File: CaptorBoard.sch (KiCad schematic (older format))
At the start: 55 parts, among them CON1 MINI-USB-SHELD-MC32598, P1 Prog, P2 POWER, Q1 IRLM6402TRPBF, SW1 CST06S08H, U1 PIC32MX795F512H-80I-PT, U2 MRF24J40MA-I-RM, U3 HTU21, U4 MPL115A2, U5 VTX-214-003-105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

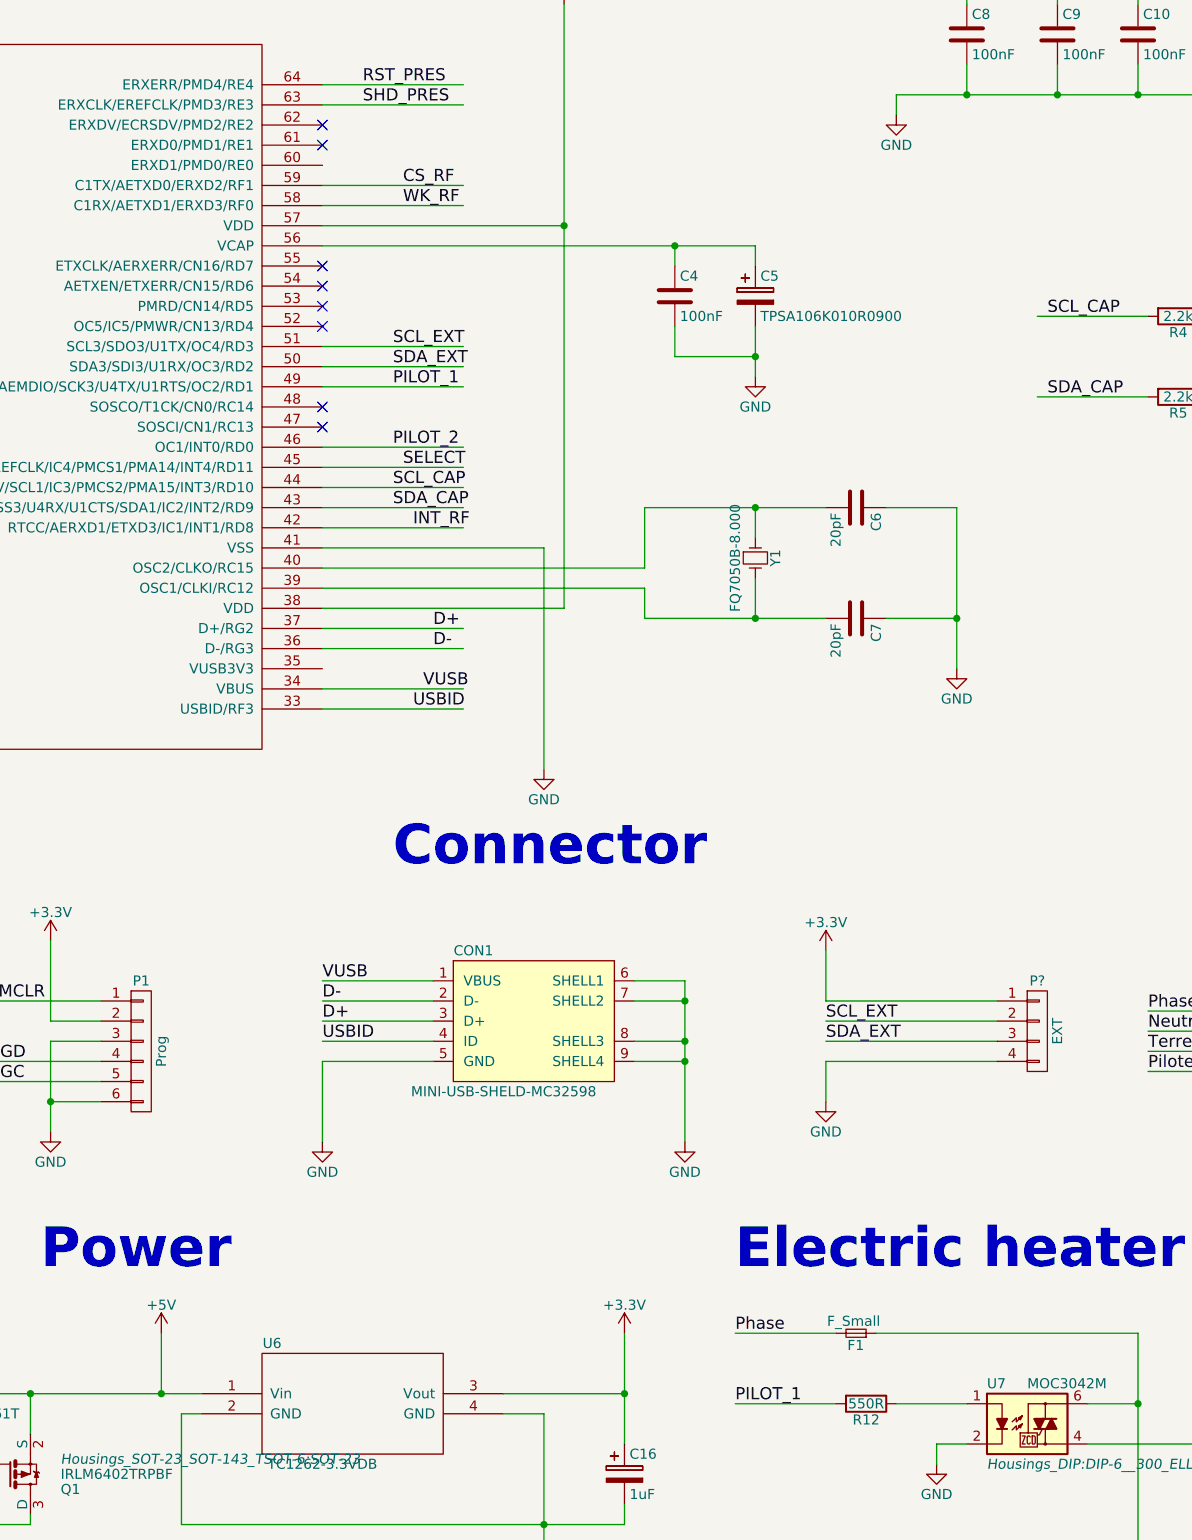
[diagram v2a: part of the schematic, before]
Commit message: Some ERC correction
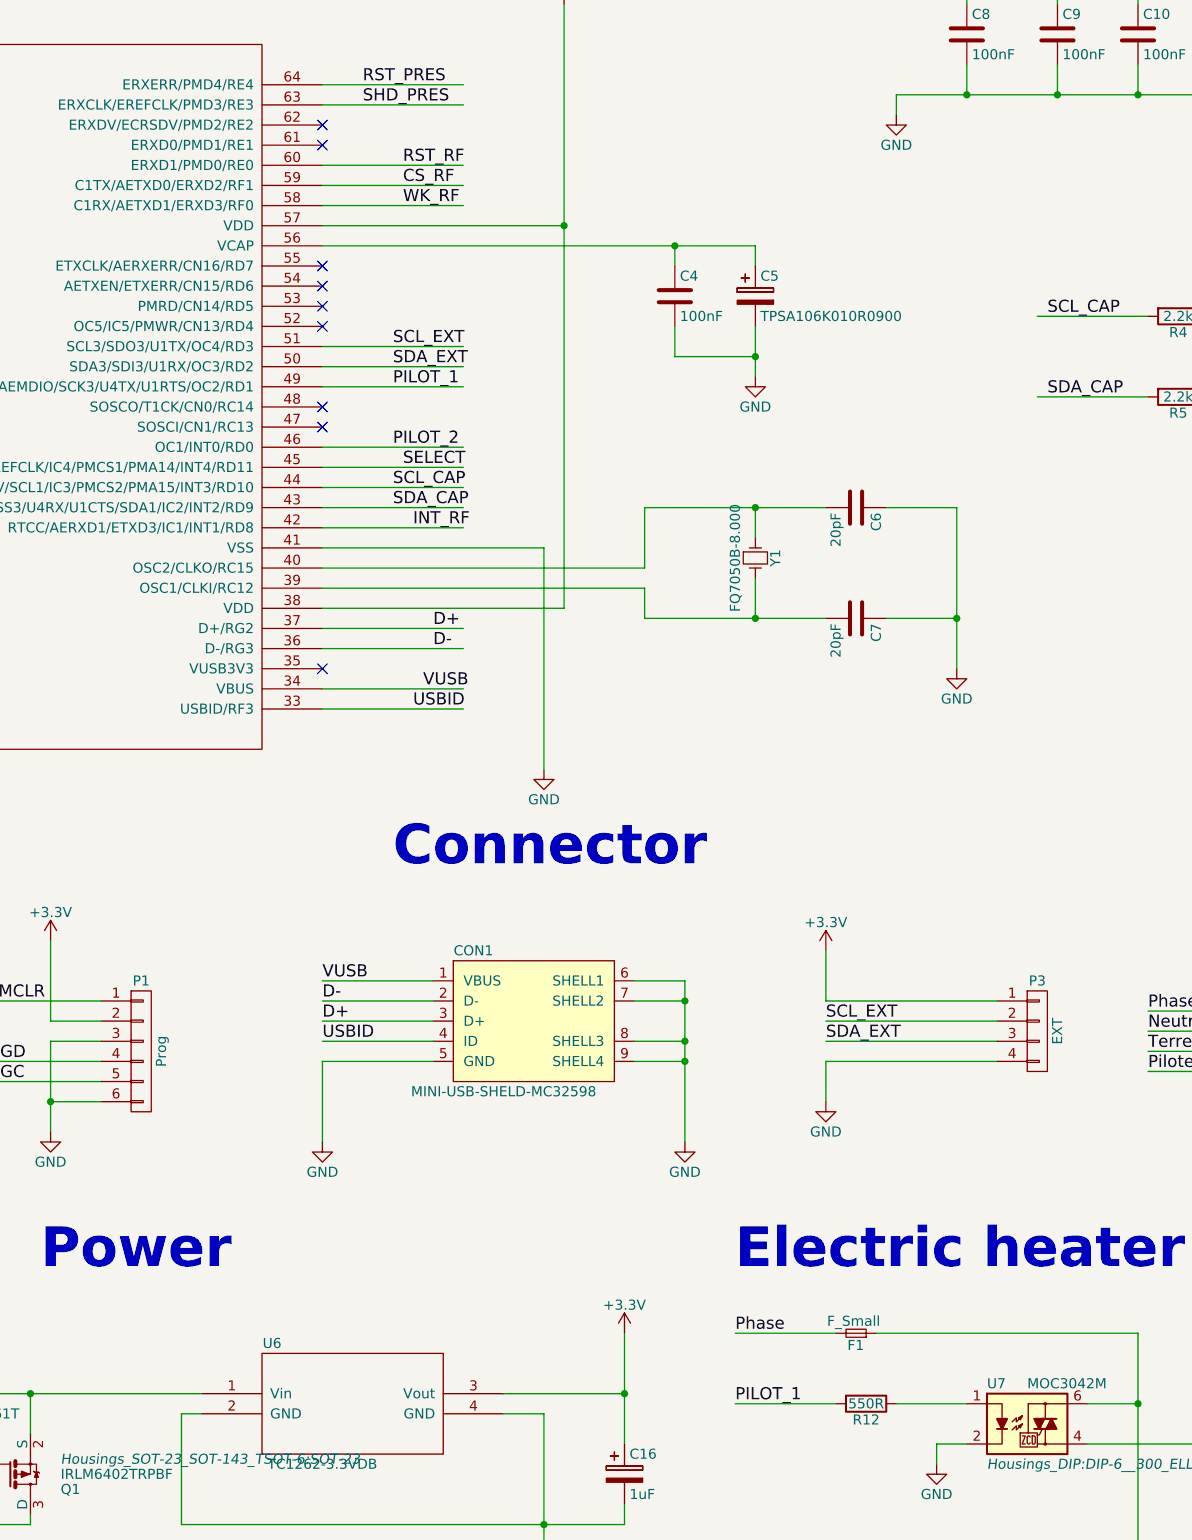
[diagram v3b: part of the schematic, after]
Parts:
- gave numbers to parts that had none: 1
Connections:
- net labels removed: +5V
- no-connect marks 23 -> 24
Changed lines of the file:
@@
-	1    0    0    -1
-$EndComp
-$Comp
-L +5V #PWR028
-U 1 1 5525FA48
-P 9800 7650
-F 0 "#PWR028" H 9800 7500 50  0001 C CNN
-F 1 "+5V" H 9800 7790 50  0000 C CNN
-F 2 "" H 9800 7650 60  0000 C CNN
-F 3 "" H 9800 7650 60  0000 C CNN
-	1    9800 7650
 	1    0    0    -1
 $EndComp
@@
 Power
 $Comp
-L GND #PWR029
+L GND #PWR028
 U 1 1 552620E9
 P 10900 10050
-F 0 "#PWR029" H 10900 9800 50  0001 C CNN
+F 0 "#PWR028" H 10900 9800 50  0001 C CNN
 F 1 "GND" H 10900 9900 50  0000 C CNN
 F 2 "" H 10900 10050 60  0000 C CNN
@@
 $EndComp
 $Comp
-L GND #PWR030
+L GND #PWR029
 U 1 1 55264B50
 P 13650 8300
-F 0 "#PWR030" H 13650 8050 50  0001 C CNN
+F 0 "#PWR029" H 13650 8050 50  0001 C CNN
 F 1 "GND" H 13650 8150 50  0000 C CNN
 F 2 "" H 13650 8300 60  0000 C CNN
@@
 $EndComp
 $Comp
-L GND #PWR031
+L GND #PWR030
 U 1 1 55264C81
 P 13650 9450
-F 0 "#PWR031" H 13650 9200 50  0001 C CNN
+F 0 "#PWR030" H 13650 9200 50  0001 C CNN
 F 1 "GND" H 13650 9300 50  0000 C CNN
 F 2 "" H 13650 9450 60  0000 C CNN
@@
 Wire Wire Line
 	9000 7950 10000 7950
-Wire Wire Line
-	9800 7950 9800 7650
-Connection ~ 9800 7950
 Wire Wire Line
 	9150 8150 9150 7950
@@
 Pilote
 $Comp
-L CONN_01X04 P?
+L CONN_01X04 P3
 U 1 1 5533F0E1
 P 14150 6150
-F 0 "P?" H 14150 6400 50  0000 C CNN
+F 0 "P3" H 14150 6400 50  0000 C CNN
 F 1 "EXT" V 14250 6150 50  0000 C CNN
 F 2 "" H 14150 6150 60  0000 C CNN
@@
 	13950 6300 13100 6300
 $Comp
-L GND #PWR?
+L GND #PWR031
 U 1 1 5533FC25
 P 13100 6500
-F 0 "#PWR?" H 13100 6250 50  0001 C CNN
+F 0 "#PWR031" H 13100 6250 50  0001 C CNN
 F 1 "GND" H 13100 6350 50  0000 C CNN
 F 2 "" H 13100 6500 60  0000 C CNN
@@
 $EndComp
 $Comp
-L +3.3V #PWR?
+L +3.3V #PWR032
 U 1 1 5533FE1F
 P 13100 5750
-F 0 "#PWR?" H 13100 5600 50  0001 C CNN
+F 0 "#PWR032" H 13100 5600 50  0001 C CNN
 F 1 "+3.3V" H 13100 5890 50  0000 C CNN
 F 2 "" H 13100 5750 60  0000 C CNN
@@
 Text Label 13100 6200 0    60   ~ 0
 SDA_EXT
+NoConn ~ 10600 4350
+Wire Wire Line
+	10600 1850 11300 1850
+Text Label 11000 1850 0    60   ~ 0
+RST_RF
 $EndSCHEMATC

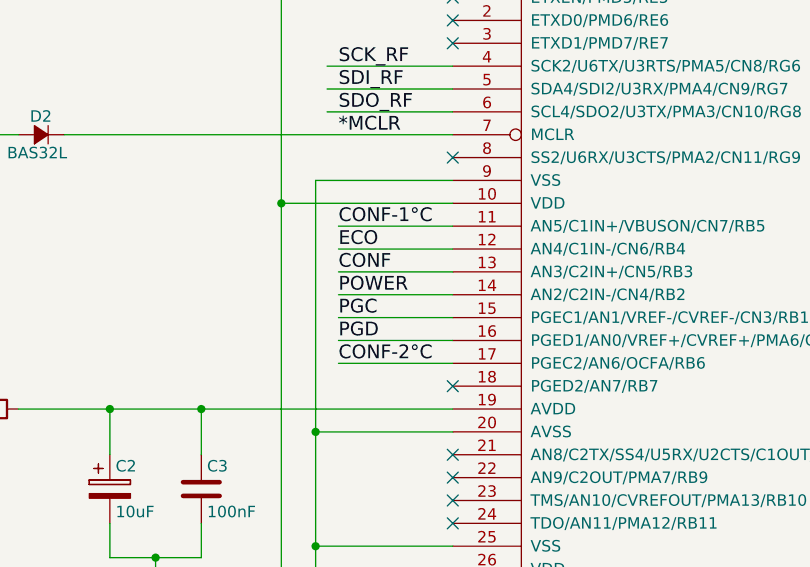
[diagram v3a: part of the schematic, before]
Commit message: Change led pin order for routing facility
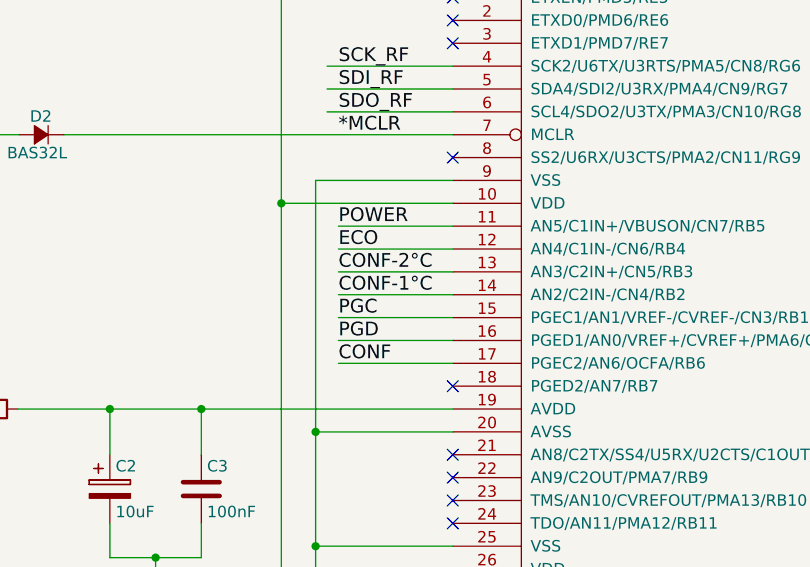
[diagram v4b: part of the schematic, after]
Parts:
- P3: footprint (none) -> Pin_Headers:Pin_Header_Straight_1x04
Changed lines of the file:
@@
 Text Label 3600 1950 0    60   ~ 0
 SDO_RF
-Text Label 3600 2450 0    60   ~ 0
+Text Label 3600 2750 0    60   ~ 0
 CONF-1°C
 Text Label 3600 2550 0    60   ~ 0
 ECO
-Text Label 3600 2650 0    60   ~ 0
+Text Label 3600 3050 0    60   ~ 0
 CONF
-Text Label 3600 2750 0    60   ~ 0
+Text Label 3600 2450 0    60   ~ 0
 POWER
 Text Label 3600 2850 0    60   ~ 0
@@
 Text Label 3600 2950 0    60   ~ 0
 PGD
-Text Label 3600 3050 0    60   ~ 0
+Text Label 3600 2650 0    60   ~ 0
 CONF-2°C
 NoConn ~ 4100 1450
@@
 	4100 1950 3550 1950
 Wire Wire Line
+	4100 2750 3600 2750
+Wire Wire Line
+	4100 2550 3600 2550
+Wire Wire Line
+	4100 3050 3600 3050
+Wire Wire Line
 	4100 2450 3600 2450
 Wire Wire Line
-	4100 2550 3600 2550
+	4100 2850 3600 2850
+Wire Wire Line
+	4100 2950 3600 2950
 Wire Wire Line
 	4100 2650 3600 2650
-Wire Wire Line
-	4100 2750 3600 2750
-Wire Wire Line
-	4100 2850 3600 2850
-Wire Wire Line
-	4100 2950 3600 2950
-Wire Wire Line
-	4100 3050 3600 3050
 Wire Wire Line
 	10600 2150 11800 2150
@@
 F 0 "P3" H 14150 6400 50  0000 C CNN
 F 1 "EXT" V 14250 6150 50  0000 C CNN
-F 2 "" H 14150 6150 60  0000 C CNN
+F 2 "Pin_Headers:Pin_Header_Straight_1x04" H 14150 6150 60  0001 C CNN
 F 3 "" H 14150 6150 60  0000 C CNN
 	1    14150 6150

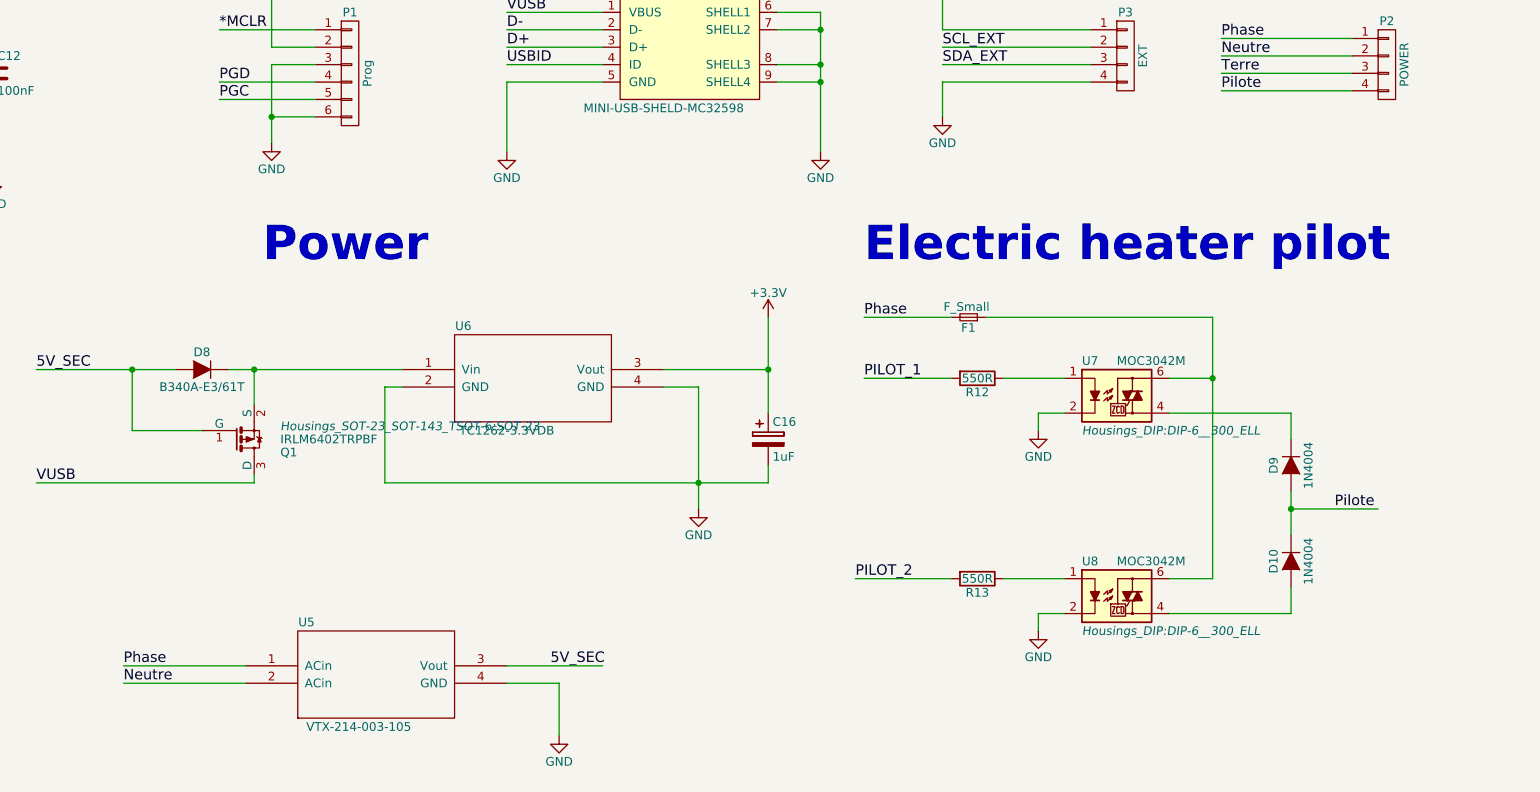
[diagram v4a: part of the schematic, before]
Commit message: Place Fuse before all
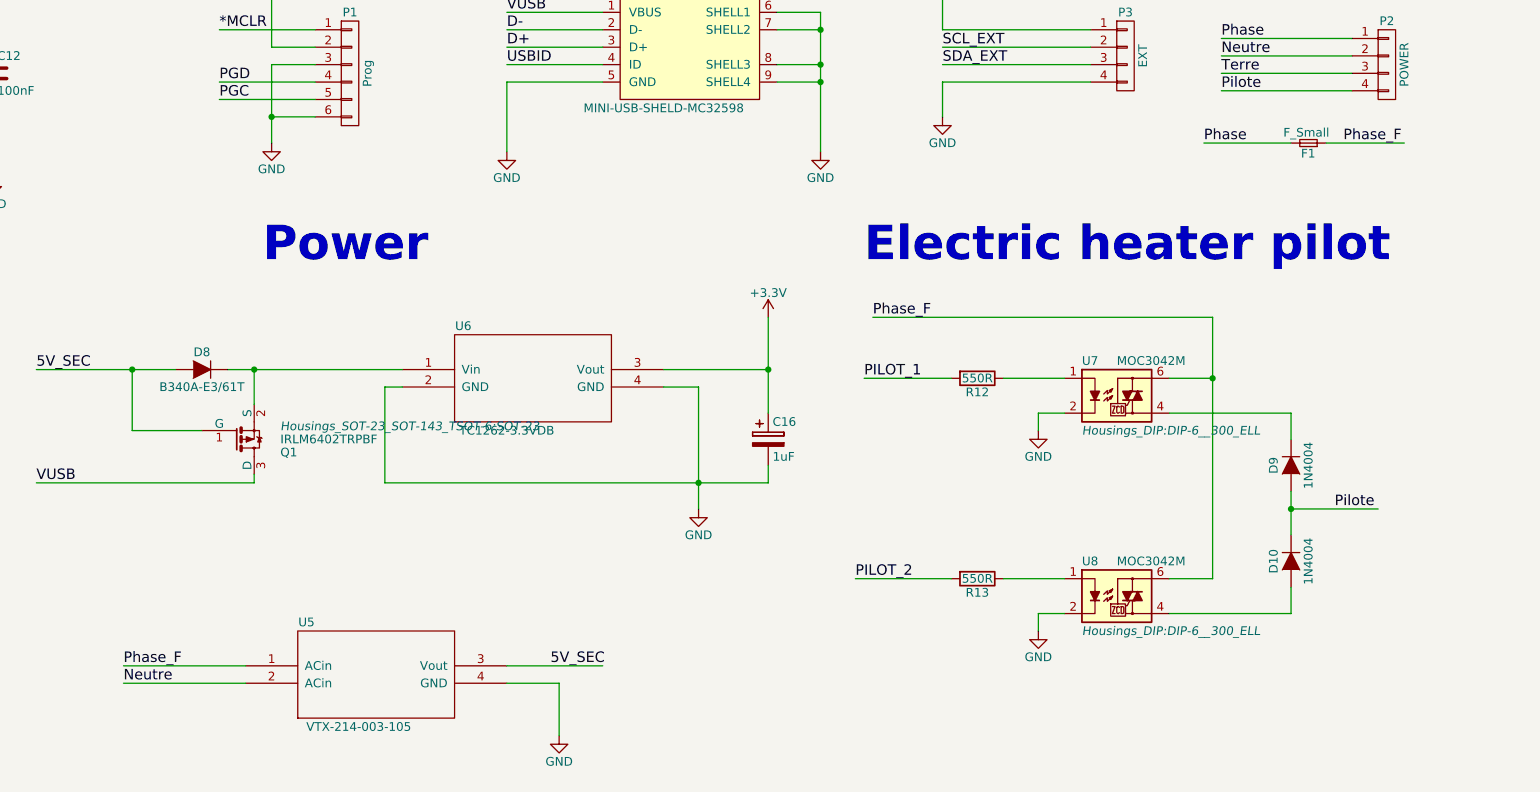
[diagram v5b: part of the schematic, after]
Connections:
- net labels added: Phase_F
- wire segments 217 -> 218
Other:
- moved on the sheet: F1
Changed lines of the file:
@@
 $EndComp
 Text Label 8400 9650 0    60   ~ 0
-Phase
+Phase_F
 Text Label 8400 9750 0    60   ~ 0
 Neutre
@@
 L F_Small F1
 U 1 1 55263FC2
-P 13250 7650
-F 0 "F1" H 13210 7710 50  0000 L CNN
-F 1 "F_Small" H 13130 7590 50  0000 L CNN
-F 2 "Fuse_Holders_and_Fuses:Fuseholder5x20_horiz_SemiClosed_Casing10x25mm" H 13250 7650 60  0001 C CNN
-F 3 "" H 13250 7650 60  0000 C CNN
-	1    13250 7650
+P 15200 6650
+F 0 "F1" H 15160 6710 50  0000 L CNN
+F 1 "F_Small" H 15080 6590 50  0000 L CNN
+F 2 "Fuse_Holders_and_Fuses:Fuseholder5x20_horiz_SemiClosed_Casing10x25mm" H 15200 6650 60  0001 C CNN
+F 3 "" H 15200 6650 60  0000 C CNN
+	1    15200 6650
 	-1   0    0    1
 $EndComp
@@
 	13150 9150 12600 9150
 Wire Wire Line
-	13350 7650 14650 7650
+	15300 6650 15750 6650
 Wire Wire Line
 	14650 7650 14650 9150
@@
 	14400 9350 15100 9350
 Wire Wire Line
-	13150 7650 12650 7650
+	15100 6650 14600 6650
 Text Notes 12650 7350 0    197  ~ 39
 Electric heater pilot
-Text Label 12650 7650 0    60   ~ 0
+Text Label 14600 6650 0    60   ~ 0
 Phase
 Text Label 12650 8000 0    60   ~ 0
@@
 Text Label 11000 1850 0    60   ~ 0
 RST_RF
+Text Label 15400 6650 0    60   ~ 0
+Phase_F
+Wire Wire Line
+	14650 7650 12700 7650
+Text Label 12700 7650 0    60   ~ 0
+Phase_F
 $EndSCHEMATC
